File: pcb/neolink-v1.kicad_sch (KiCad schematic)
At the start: 11 parts, among them J1 ESP32_Connector_2x16, J10 SMA_Antenna, J2 SIM800L_HDR_1x6, J3 MAX31865_1_HDR_2x4, J4 MAX31865_2_HDR_2x4, J5 SHT35_1_JST_XH_4p, J6 SHT35_2_JST_XH_4p, J7 PT100_1_JST_XH_2p, J8 PT100_2_JST_XH_2p, J9 LiPo_JST_XH_2p

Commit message: fix(pcb): agrega PWR_FLAG en GND, VCC_3V3, VCC_5V, BAT — ERC limpio
Co-authored-by: Cursor <cursoragent@cursor.com>
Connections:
- net GND is gone; now on net PWR: C1.1 (+), J1.1 (GND), J1.2 (GND), J3.2 (GND), J4.2 (GND)
- net ~{VCC_3V3} is gone; now on net PWR: J3.1 (~{VCC_3V3}), J4.1 (~{VCC_3V3}), J5.1 (~{VCC_3V3}), J6.1 (~{VCC_3V3})
- net ~{VCC_5V} is gone; now on net PWR: C1.2 (-), J2.1 (~{VCC_5V})
- net BAT renamed PWR
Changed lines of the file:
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@@
   (pin "2")
+)
+(symbol (lib_id "PWR_FLAG") (at 30 10 0) (unit 1)
+  (in_bom yes) (on_board yes) (dnp no)
+  (property "Reference" "#PWR01" (at 0 -3.81 0) (effects (font (size 1.27 1.27)) hide))
+  (property "Value" "PWR_FLAG" (at 0 -2.54 0) (effects (font (size 1.27 1.27))))
+  (property "Footprint" "" (at 0 0 0) (effects (font (size 1.27 1.27)) hide))
+  (pin "1")
+)
+(symbol (lib_id "PWR_FLAG") (at 30 20 0) (unit 1)
+  (in_bom yes) (on_board yes) (dnp no)
+  (property "Reference" "#PWR02" (at 0 -3.81 0) (effects (font (size 1.27 1.27)) hide))
+  (property "Value" "PWR_FLAG" (at 0 -2.54 0) (effects (font (size 1.27 1.27))))
+  (property "Footprint" "" (at 0 0 0) (effects (font (size 1.27 1.27)) hide))
+  (pin "1")
+)
+(symbol (lib_id "PWR_FLAG") (at 30 30 0) (unit 1)
+  (in_bom yes) (on_board yes) (dnp no)
+  (property "Reference" "#PWR03" (at 0 -3.81 0) (effects (font (size 1.27 1.27)) hide))
+  (property "Value" "PWR_FLAG" (at 0 -2.54 0) (effects (font (size 1.27 1.27))))
+  (property "Footprint" "" (at 0 0 0) (effects (font (size 1.27 1.27)) hide))
+  (pin "1")
+)
+(symbol (lib_id "PWR_FLAG") (at 30 40 0) (unit 1)
+  (in_bom yes) (on_board yes) (dnp no)
+  (property "Reference" "#PWR04" (at 0 -3.81 0) (effects (font (size 1.27 1.27)) hide))
+  (property "Value" "PWR_FLAG" (at 0 -2.54 0) (effects (font (size 1.27 1.27))))
+  (property "Footprint" "" (at 0 0 0) (effects (font (size 1.27 1.27)) hide))
+  (pin "1")
 )
 (symbol (lib_id "C_TH") (at 140 55 0) (unit 1)
@@
   (pin "~")
 )
+(global_label "GND" (shape bidirectional) (at 24.92 10 0)
+  (effects (font (size 1.27 1.27)))
+  (property "Intersheet References" "${INTERSHEET_REFS}" (at 0 0 0) (effects (font (size 1.27 1.27)) hide))
+  (pin "~")
+)
+(global_label "~{VCC_3V3}" (shape bidirectional) (at 24.92 20 0)
+  (effects (font (size 1.27 1.27)))
+  (property "Intersheet References" "${INTERSHEET_REFS}" (at 0 0 0) (effects (font (size 1.27 1.27)) hide))
+  (pin "~")
+)
+(global_label "~{VCC_5V}" (shape bidirectional) (at 24.92 30 0)
+  (effects (font (size 1.27 1.27)))
+  (property "Intersheet References" "${INTERSHEET_REFS}" (at 0 0 0) (effects (font (size 1.27 1.27)) hide))
+  (pin "~")
+)
+(global_label "BAT" (shape bidirectional) (at 24.92 40 0)
+  (effects (font (size 1.27 1.27)))
+  (property "Intersheet References" "${INTERSHEET_REFS}" (at 0 0 0) (effects (font (size 1.27 1.27)) hide))
+  (pin "~")
+)
 (global_label "~{VCC_5V}" (shape bidirectional) (at 140 63.89 270)
   (effects (font (size 1.27 1.27)))
@@
   (stroke (width 0) (type default))
 )
+(wire (pts (xy 24.92 10) (xy 30 10))
+  (stroke (width 0) (type default))
+)
+(wire (pts (xy 24.92 20) (xy 30 20))
+  (stroke (width 0) (type default))
+)
+(wire (pts (xy 24.92 30) (xy 30 30))
+  (stroke (width 0) (type default))
+)
+(wire (pts (xy 24.92 40) (xy 30 40))
+  (stroke (width 0) (type default))
+)

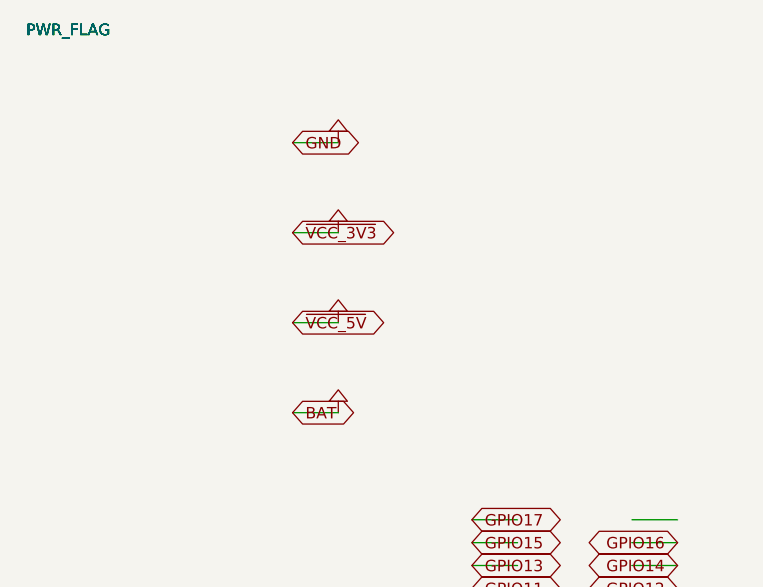
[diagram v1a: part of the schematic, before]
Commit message: fix: corregir formato KiCad para compatibilidad con KiCad 10
- Actualizar versión del esquemático a 20231120 con generator_version 8.0
- Eliminar (pin "~" ...) de global_label (no válido en KiCad 10)
- Eliminar polilínea fill(filled) del PWR_FLAG que rompía el parser
- Esquemático ahora carga y pasa ERC en kicad-cli 10.0.3

Co-authored-by: Cursor <cursoragent@cursor.com>
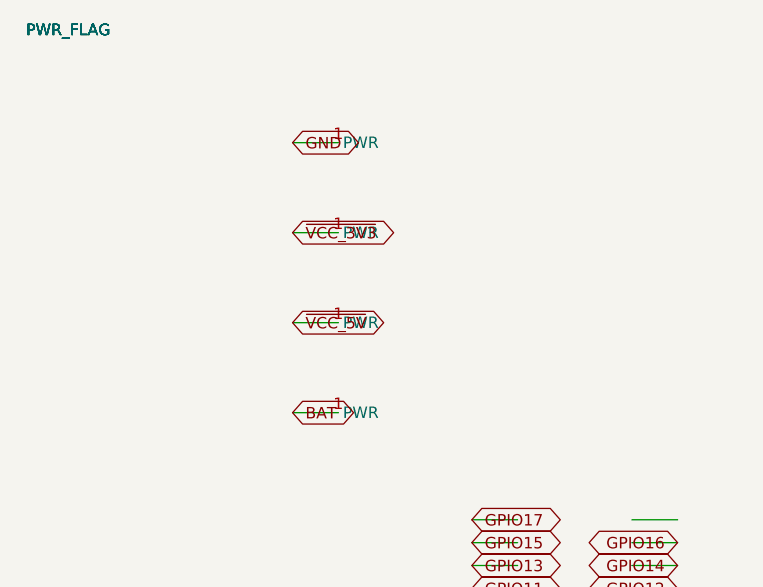
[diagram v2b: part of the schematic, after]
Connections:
- net PWR renamed PWR_FLAG

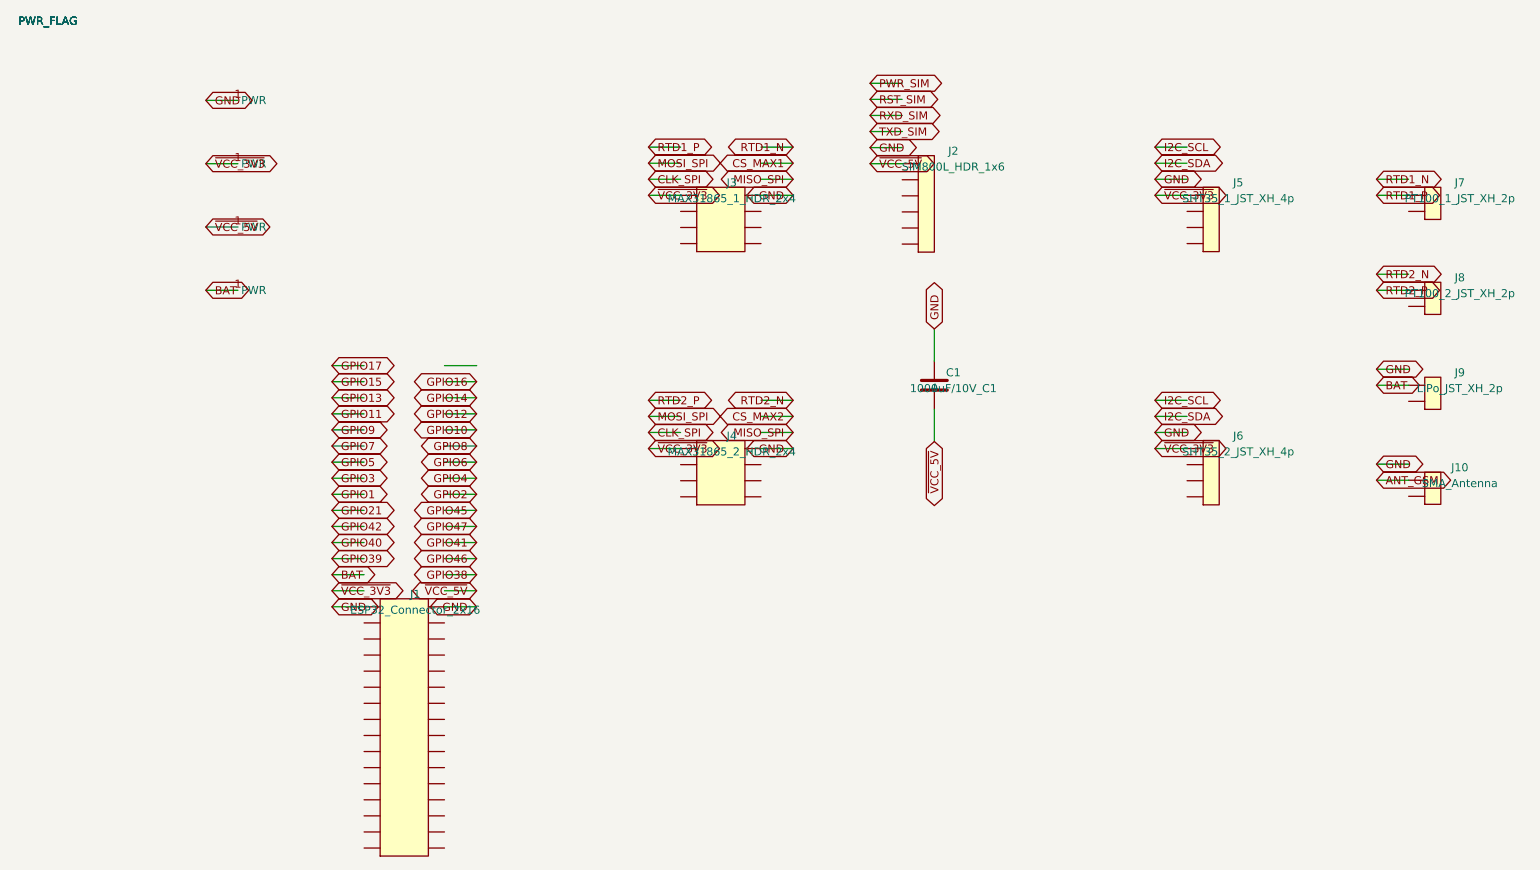
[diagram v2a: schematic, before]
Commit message: fix: ERC pasa limpio (0 errores) — coordenadas de pines corregidas
Causa raíz: KiCad aplica y-flip al colocar símbolos (y_abs = sym_y - pin_y).
Las funciones attach_1x/attach_2x usaban ay-i*2.54 cuando deben ser ay+i*2.54.

Cambios en gen.py:
- attach_1x/attach_2x: dirección Y corregida (- → +)
- Capacitor: wires VCC_5V sube / GND baja (evita T-junction)
- PWR_FLAG: pin power_in → power_out (ERC power_pin_not_driven)
- NC pins: genera (no_connect ...) en lugar de wire huérfano
- Agrega lista NOCONNECTS al output del esquemático

Nuevo fix_schematic.py: wrapper que llama gen.py y verifica ERC automáticamente.
ERC final: 0 errores, 0 warnings (kicad-cli 10.0.3)

Co-authored-by: Cursor <cursoragent@cursor.com>
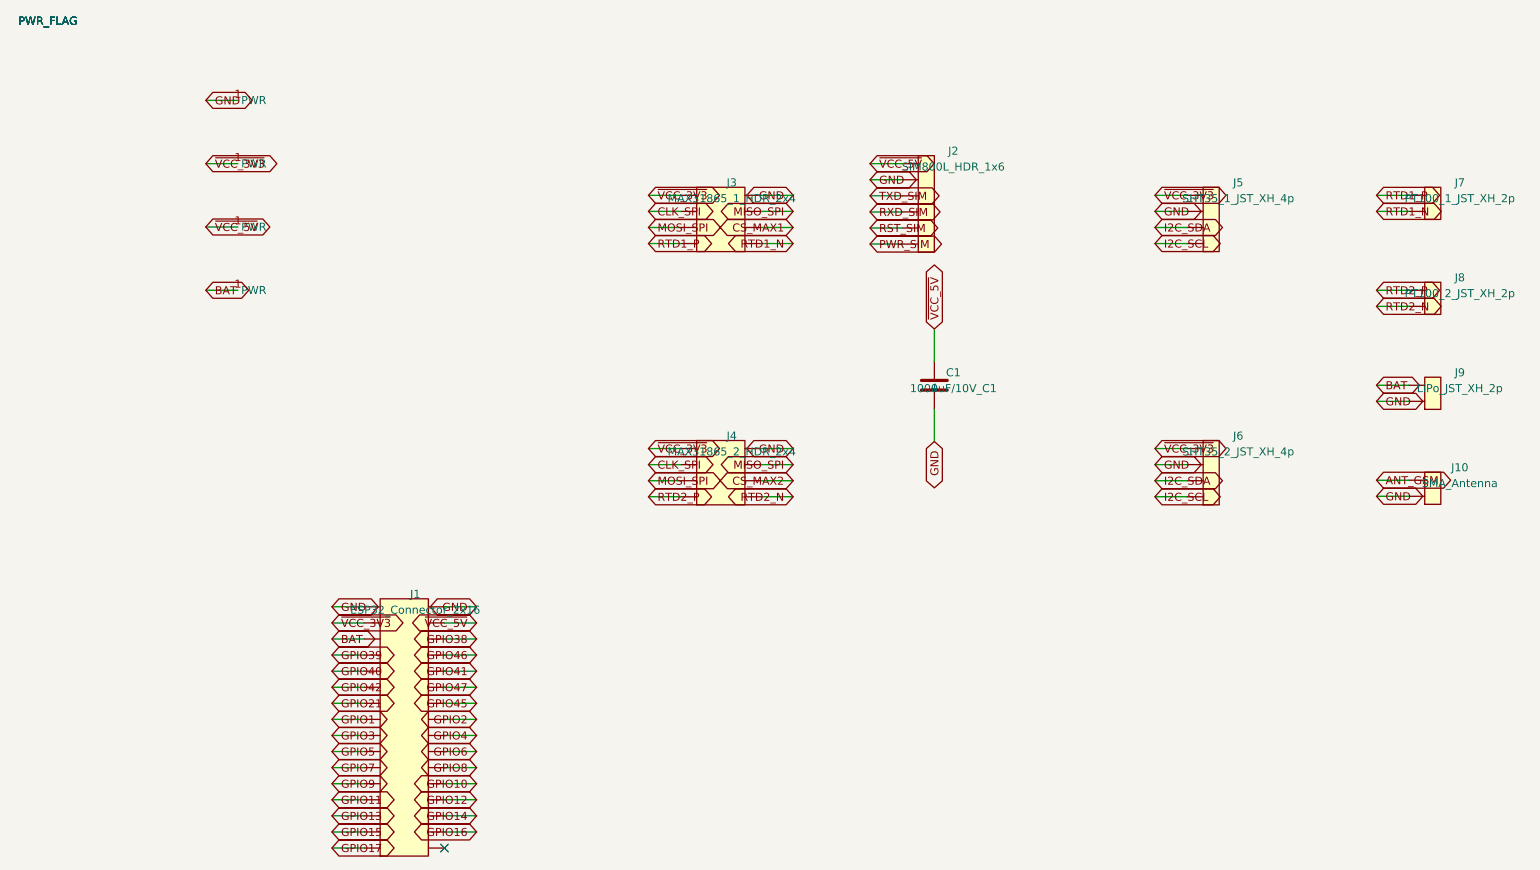
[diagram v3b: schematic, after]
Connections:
- net CLK_SPI: now also J3.3 (CLK_SPI), J4.3 (CLK_SPI)
- net CS_MAX1: now also J3.6 (CS_MAX1)
- net CS_MAX2: now also J4.6 (CS_MAX2)
- net GPIO1: now also J1.15 (GPIO1)
- net GPIO10: now also J1.24 (GPIO10)
- net GPIO11: now also J1.25 (GPIO11)
- net GPIO12: now also J1.26 (GPIO12)
- net GPIO13: now also J1.27 (GPIO13)
- net GPIO14: now also J1.28 (GPIO14)
- net GPIO15: now also J1.29 (GPIO15)
- net GPIO16: now also J1.30 (GPIO16)
- net GPIO17: now also J1.31 (GPIO17)
- net GPIO2: now also J1.16 (GPIO2)
- net GPIO21: now also J1.13 (GPIO21)
- net GPIO3: now also J1.17 (GPIO3)
- net GPIO38: now also J1.6 (GPIO38)
- net GPIO39: now also J1.7 (GPIO39)
- net GPIO4: now also J1.18 (GPIO4)
- net GPIO40: now also J1.9 (GPIO40)
- net GPIO41: now also J1.10 (GPIO41)
- net GPIO42: now also J1.11 (GPIO42)
- net GPIO45: now also J1.14 (GPIO45)
- net GPIO46: now also J1.8 (GPIO46)
- net GPIO47: now also J1.12 (GPIO47)
- net GPIO5: now also J1.19 (GPIO5)
- net GPIO6: now also J1.20 (GPIO6)
- net GPIO7: now also J1.21 (GPIO7)
- net GPIO8: now also J1.22 (GPIO8)
- net GPIO9: now also J1.23 (GPIO9)
- net I2C_SCL: now also J5.4 (I2C_SCL), J6.4 (I2C_SCL)
- net I2C_SDA: now also J5.3 (I2C_SDA), J6.3 (I2C_SDA)
- net MISO_SPI: now also J3.4 (MISO_SPI), J4.4 (MISO_SPI)
- net MOSI_SPI: now also J3.5 (MOSI_SPI), J4.5 (MOSI_SPI)
- net PWR_SIM: now also J2.6 (PWR_SIM)
- net RST_SIM: now also J2.5 (RST_SIM)
- net RTD1_N: now also J3.8 (RTD1_N), J7.2 (RTD1_N)
- net RTD1_P: now also J3.7 (RTD1_P)
- net RTD2_N: now also J4.8 (RTD2_N), J8.2 (RTD2_N)
- net RTD2_P: now also J4.7 (RTD2_P)
- net RXD_SIM: now also J2.4 (RXD_SIM)
- net TXD_SIM: now also J2.3 (TXD_SIM)
- net GND: now reaches J10.2 (GND)
- net GND: now also C1.2 (-), J1.1 (GND), J1.2 (GND), J2.2 (GND), J3.2 (GND), J4.2 (GND), J5.2 (GND), J6.2 (GND), J9.2 (GND)
- net ~{VCC_3V3}: now reaches J1.3 (~{VCC_3V3})
- net ~{VCC_3V3}: now also J3.1 (~{VCC_3V3}), J4.1 (~{VCC_3V3}), J5.1 (~{VCC_3V3}), J6.1 (~{VCC_3V3})
- net ~{VCC_5V}: now reaches J1.4 (~{VCC_5V})
- net ~{VCC_5V}: now also C1.1 (+), J2.1 (~{VCC_5V})
- net BAT: now reaches J1.5 (BAT)
- net BAT: now also J9.1 (BAT)
- removed net PWR_FLAG: C1.1 (+), C1.2 (-), J1.1 (GND), J1.2 (GND), J2.1 (~{VCC_5V}), J3.1 (~{VCC_3V3}), J3.2 (GND), J4.1 (~{VCC_3V3}), J4.2 (GND), J5.1 (~{VCC_3V3}), J6.1 (~{VCC_3V3}), J9.1 (BAT)
- no-connect marks 0 -> 1

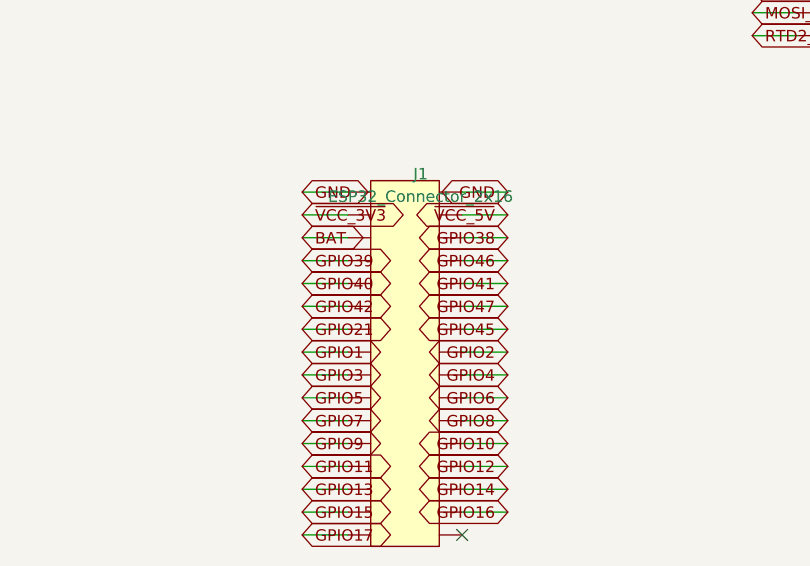
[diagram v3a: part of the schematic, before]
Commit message: Add KiCad PCB layout with complete routing and DRC pass
- Component placement: J1 ESP32 center, J2 SIM800L right (y-aligned to J1 row midpoints),
  J3/J4 MAX31865 left, J5/J6 SHT35 right, J7/J8 PT100 top-right,
  J9 LiPo bottom-left, J10 SMA bottom-right, C1 cap next to SIM800L
- Board outline: 110×80 mm
- F.Cu routing: power nets (VCC_3V3/5V/GND/BAT) at 1.0 mm, signal nets at 0.5 mm
- B.Cu: GND copper pour
- DRC: 0 shorts, 0 unconnected, 0 clearance violations (44 tracks_crossing — unavoidable single-layer)
- Pad size reduced to 1.3 mm/0.8 mm drill for routing clearance between 2.54 mm header rows
- Euclidean clearance check and trace-width-aware collision detection in gen.py router

Co-authored-by: Cursor <cursoragent@cursor.com>
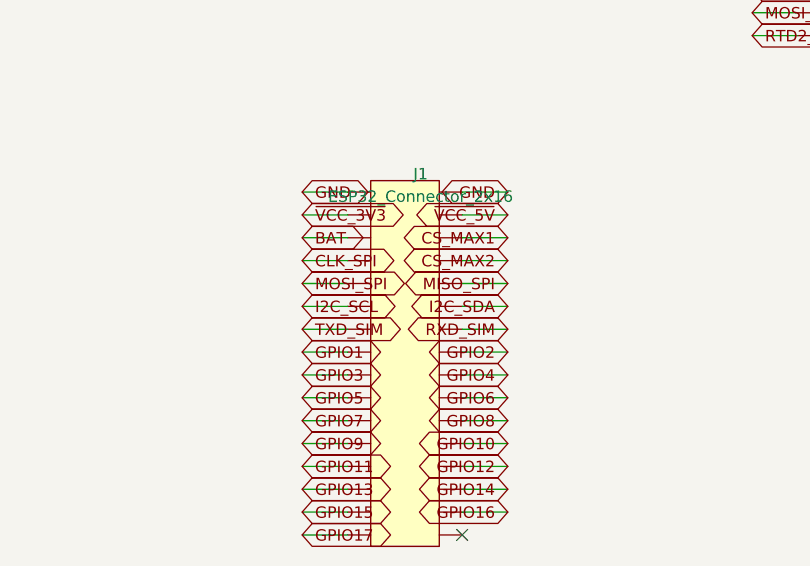
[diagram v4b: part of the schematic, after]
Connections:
- net GPIO21 is gone; now on net TXD_SIM: J1.13 (TXD_SIM)
- net GPIO38 is gone; now on net CS_MAX1: J1.6 (CS_MAX1)
- net GPIO39 is gone; now on net CLK_SPI: J1.7 (CLK_SPI)
- net GPIO40 is gone; now on net MOSI_SPI: J1.9 (MOSI_SPI)
- net GPIO41 is gone; now on net MISO_SPI: J1.10 (MISO_SPI)
- net GPIO42 is gone; now on net I2C_SCL: J1.11 (I2C_SCL)
- net GPIO45 is gone; now on net RXD_SIM: J1.14 (RXD_SIM)
- net GPIO46 is gone; now on net CS_MAX2: J1.8 (CS_MAX2)
- net GPIO47 is gone; now on net I2C_SDA: J1.12 (I2C_SDA)
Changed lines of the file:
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@@
   (effects (font (size 1.27 1.27)))
 )
-(global_label "GPIO38" (shape bidirectional) (at 67.7 95.08 180)
+(global_label "CS_MAX1" (shape bidirectional) (at 67.7 95.08 180)
   (effects (font (size 1.27 1.27)))
 )
-(global_label "GPIO39" (shape bidirectional) (at 44.84 97.62 0)
+(global_label "CLK_SPI" (shape bidirectional) (at 44.84 97.62 0)
   (effects (font (size 1.27 1.27)))
 )
-(global_label "GPIO46" (shape bidirectional) (at 67.7 97.62 180)
+(global_label "CS_MAX2" (shape bidirectional) (at 67.7 97.62 180)
   (effects (font (size 1.27 1.27)))
 )
-(global_label "GPIO40" (shape bidirectional) (at 44.84 100.16 0)
+(global_label "MOSI_SPI" (shape bidirectional) (at 44.84 100.16 0)
   (effects (font (size 1.27 1.27)))
 )
-(global_label "GPIO41" (shape bidirectional) (at 67.7 100.16 180)
+(global_label "MISO_SPI" (shape bidirectional) (at 67.7 100.16 180)
   (effects (font (size 1.27 1.27)))
 )
-(global_label "GPIO42" (shape bidirectional) (at 44.84 102.7 0)
+(global_label "I2C_SCL" (shape bidirectional) (at 44.84 102.7 0)
   (effects (font (size 1.27 1.27)))
 )
-(global_label "GPIO47" (shape bidirectional) (at 67.7 102.7 180)
+(global_label "I2C_SDA" (shape bidirectional) (at 67.7 102.7 180)
   (effects (font (size 1.27 1.27)))
 )
-(global_label "GPIO21" (shape bidirectional) (at 44.84 105.24 0)
+(global_label "TXD_SIM" (shape bidirectional) (at 44.84 105.24 0)
   (effects (font (size 1.27 1.27)))
 )
-(global_label "GPIO45" (shape bidirectional) (at 67.7 105.24 180)
+(global_label "RXD_SIM" (shape bidirectional) (at 67.7 105.24 180)
   (effects (font (size 1.27 1.27)))
 )

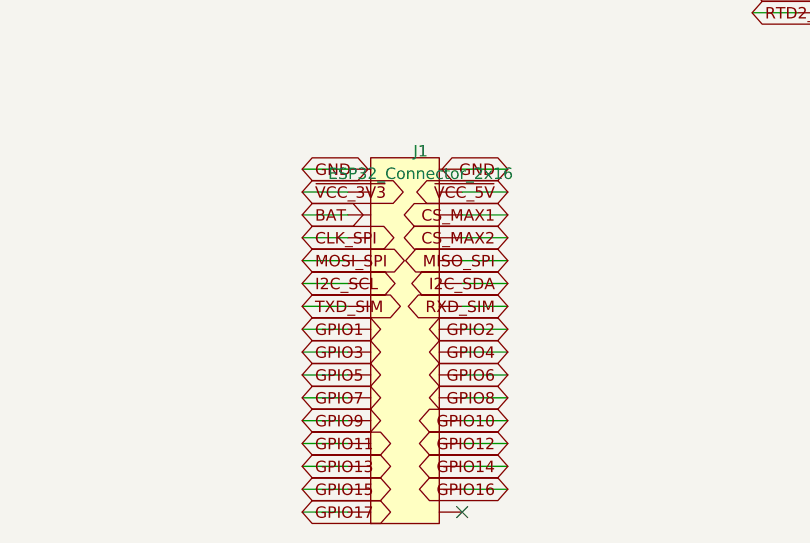
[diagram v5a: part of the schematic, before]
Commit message: PCB: complete 0-FALLBACK routing on 50×80mm portrait layout
- Fix J3_YRANGE hint bug: add x<15 guard to prevent VCC_5V getting
  spurious F.Cu hint (was blocking B.Cu corridors across the board)
- Remove J3→J4 F.Cu hint: let SPI hops choose layer freely, freeing
  F.Cu for I2C via routes
- Swap I2C_SDA/SCL in ESP32_PINS: SDA on left col (x=2.54) enables
  leftward B.Cu escape toward vias without hitting SPI pads
- Add 1.25 mm to all jog/S-bend offset candidates (_DX, _DY, C/D/E+F)
  enabling exact clearance approach to 2.50 mm pitch JST pads
- EARLY_NETS: add I2C_SDA/SCL (claim B.Cu corridors before CS_MAX2),
  add RTD1_N; remove CS_MAX2 (now routes cleanly in rest order)
- FORCE_FCU: only RTD1_N (frees middle B.Cu corridor for I2C vias)
- 0 FALLBACKs, 0 unconnected items, 0 electrical DRC violations

Co-authored-by: Cursor <cursoragent@cursor.com>
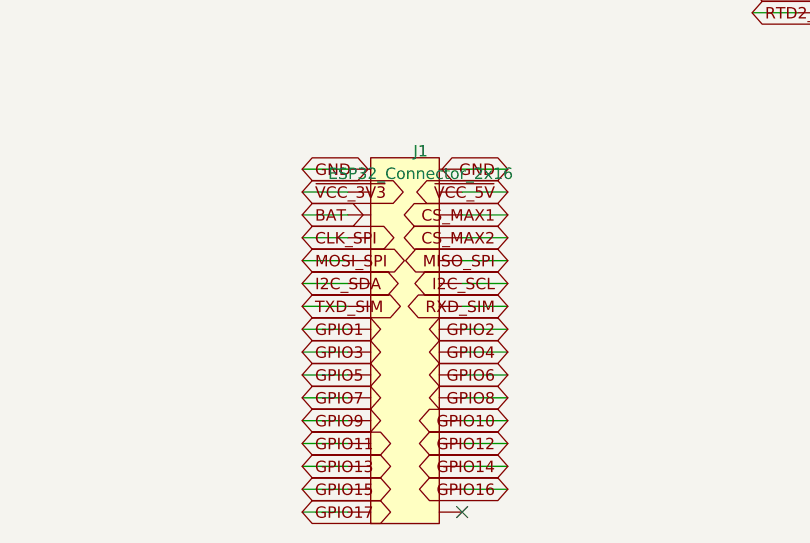
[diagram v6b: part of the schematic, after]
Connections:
- net I2C_SCL: now also J1.12 (I2C_SCL); no longer J1.11 (I2C_SCL)
- net I2C_SDA: now also J1.11 (I2C_SDA); no longer J1.12 (I2C_SDA)
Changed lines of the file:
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@@
   (effects (font (size 1.27 1.27)))
 )
-(global_label "I2C_SCL" (shape bidirectional) (at 44.84 102.7 0)
+(global_label "I2C_SDA" (shape bidirectional) (at 44.84 102.7 0)
   (effects (font (size 1.27 1.27)))
 )
-(global_label "I2C_SDA" (shape bidirectional) (at 67.7 102.7 180)
+(global_label "I2C_SCL" (shape bidirectional) (at 67.7 102.7 180)
   (effects (font (size 1.27 1.27)))
 )
